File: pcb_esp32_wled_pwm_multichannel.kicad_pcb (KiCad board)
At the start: 4 copper layers, 162.6 x 48.3 mm, 93 parts, among them J101 WJ2EDGRC-5.08-4P, J102 WJ2EDGRC-5.08-4P, J103 WJ2EDGRC-5.08-4P, J104 WJ2EDGRC-5.08-4P, J105 Conn_01x05_Male, J106 Conn_01x03_Female, J107 Conn_01x03_Female, J108 Conn_01x02_Female, J109 USB_C_Receptacle_USB2.0, Q101 IRLR8743TRPBF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

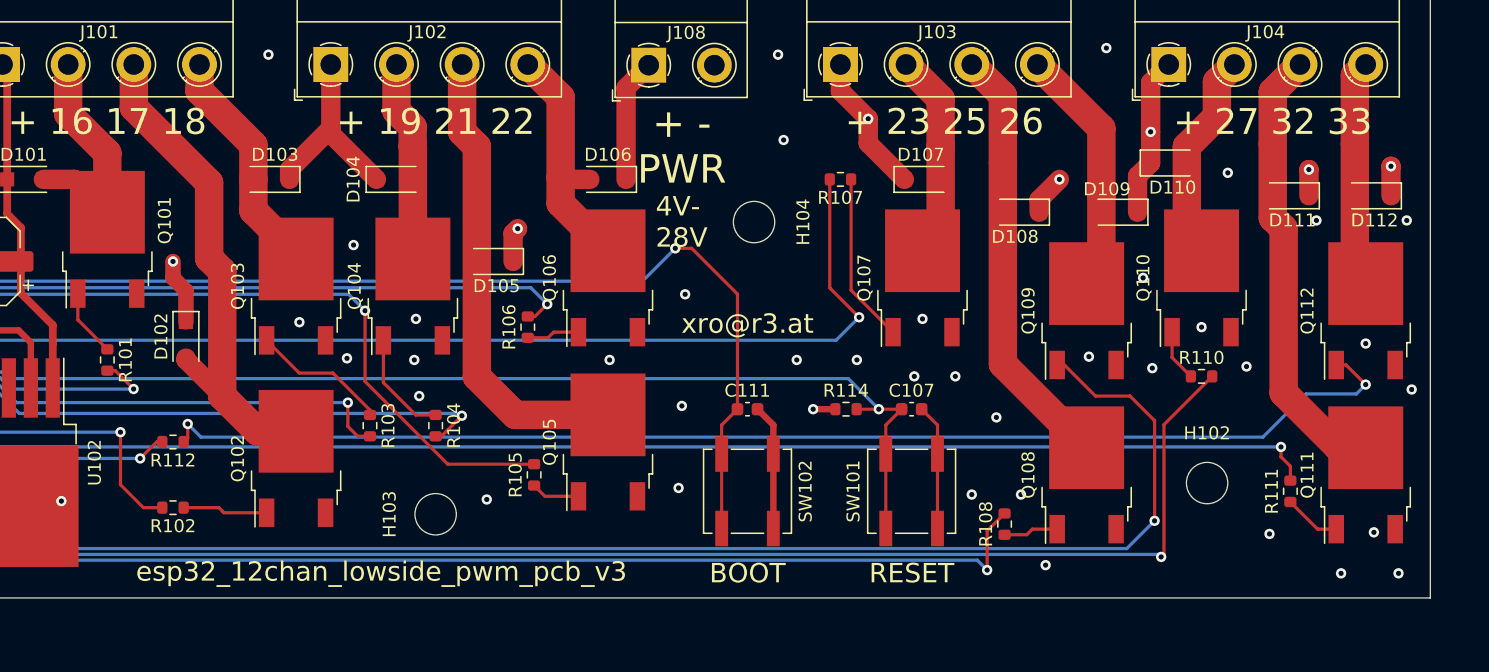
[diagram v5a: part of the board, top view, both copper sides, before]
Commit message: wip: re-add 10ks discharge R to MosFETs
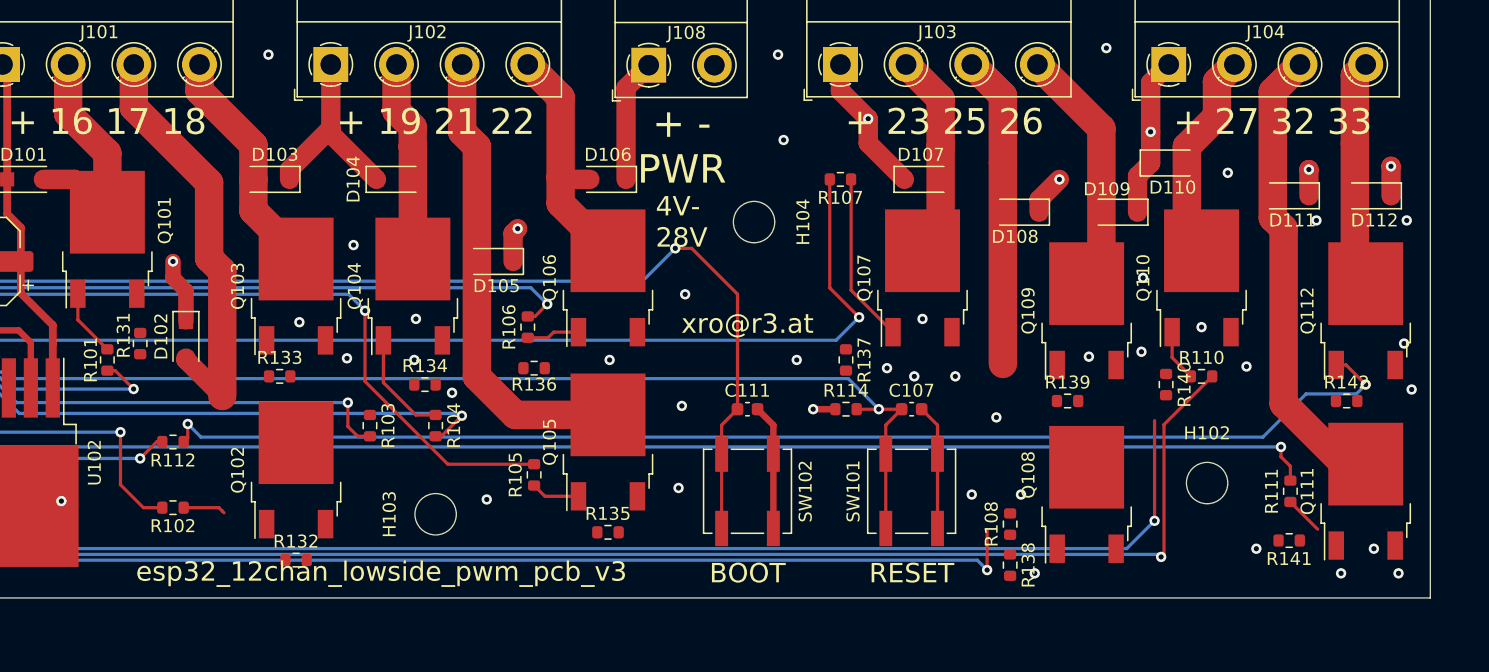
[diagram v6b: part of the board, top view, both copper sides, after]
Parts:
- added R131: 10K(5%), Resistor_SMD:R_0603_1608Metric, F.Cu at (72.4, 66.0)
- added R132: 10K(5%), Resistor_SMD:R_0603_1608Metric, F.Cu at (84.5, 82.8)
- added R133: 10K(5%), Resistor_SMD:R_0603_1608Metric, F.Cu at (83.2, 68.6)
- added R134: 10K(5%), Resistor_SMD:R_0603_1608Metric, F.Cu at (94.4, 69.2)
- added R135: 10K(5%), Resistor_SMD:R_0603_1608Metric, F.Cu at (108.6, 80.6)
- added R136: 10K(5%), Resistor_SMD:R_0603_1608Metric, F.Cu at (102.9, 67.9)
- added R137: 10K(5%), Resistor_SMD:R_0603_1608Metric, F.Cu at (127.0, 67.3)
- added R138: 10K(5%), Resistor_SMD:R_0603_1608Metric, F.Cu at (139.7, 83.2)
- added R139: 10K(5%), Resistor_SMD:R_0603_1608Metric, F.Cu at (144.1, 70.5)
- added R140: 10K(5%), Resistor_SMD:R_0603_1608Metric, F.Cu at (151.8, 69.2)
- added R141: 10K(5%), Resistor_SMD:R_0603_1608Metric, F.Cu at (161.3, 81.3)
- added R142: 10K(5%), Resistor_SMD:R_0603_1608Metric, F.Cu at (165.7, 70.5)
- moved Q108 1.52 mm to (145.6, 77.7)
- moved Q111 1.27 mm to (167.2, 77.5)
- moved Q102 0.88 mm to (84.5, 75.8)
- moved R108 0.43 mm to (139.7, 80.0)
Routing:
- net Net-(Q103-G): track 10.6 -> 0.00 mm
- net Net-(Q109-G): track 142.8 -> 133.5 mm
- net /LED_G3: track 33.3 -> 24.2 mm
- net /LED_G1: track 39.4 -> 32.6 mm
- net Net-(Q108-G): track 4.25 -> 0.00 mm
- net Net-(Q102-G): track 6.58 -> 3.28 mm
- net /PWM_G3: track 123.4 -> 121.5 mm
- net Net-(Q111-G): track 4.42 -> 2.98 mm
- net /LED_G4: track 34.7 -> 35.8 mm

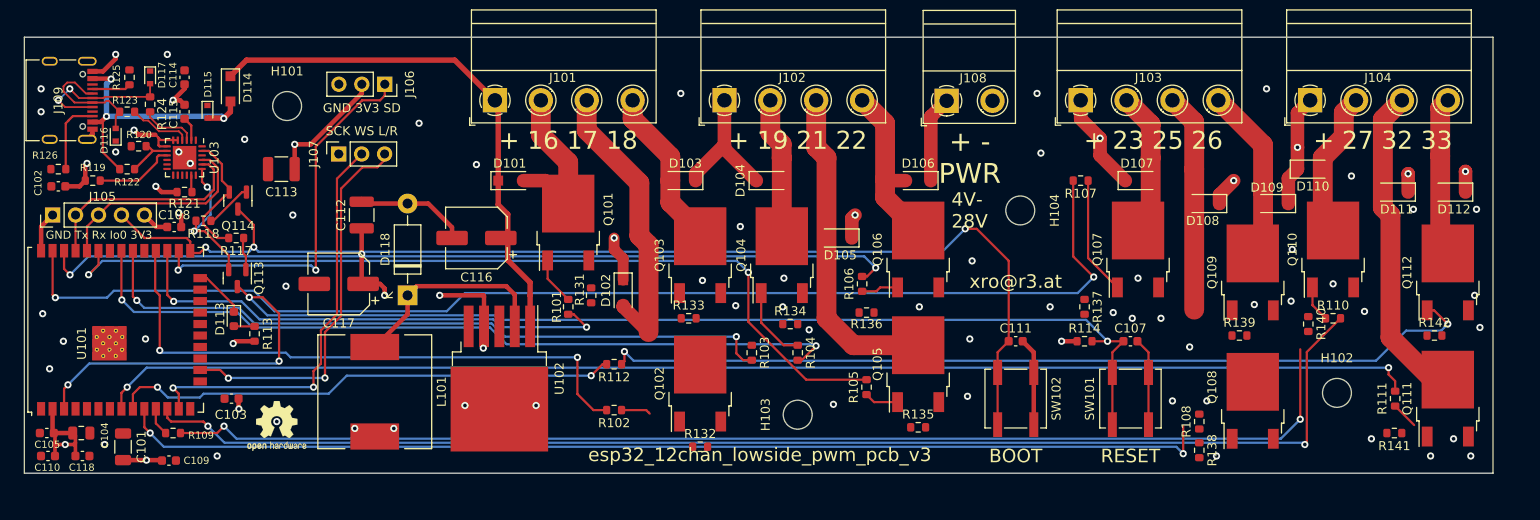
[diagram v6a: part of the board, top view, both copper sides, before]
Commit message: v3 release version: improved routing, closer C, WIP discharge-R done, new renderings, new gerber
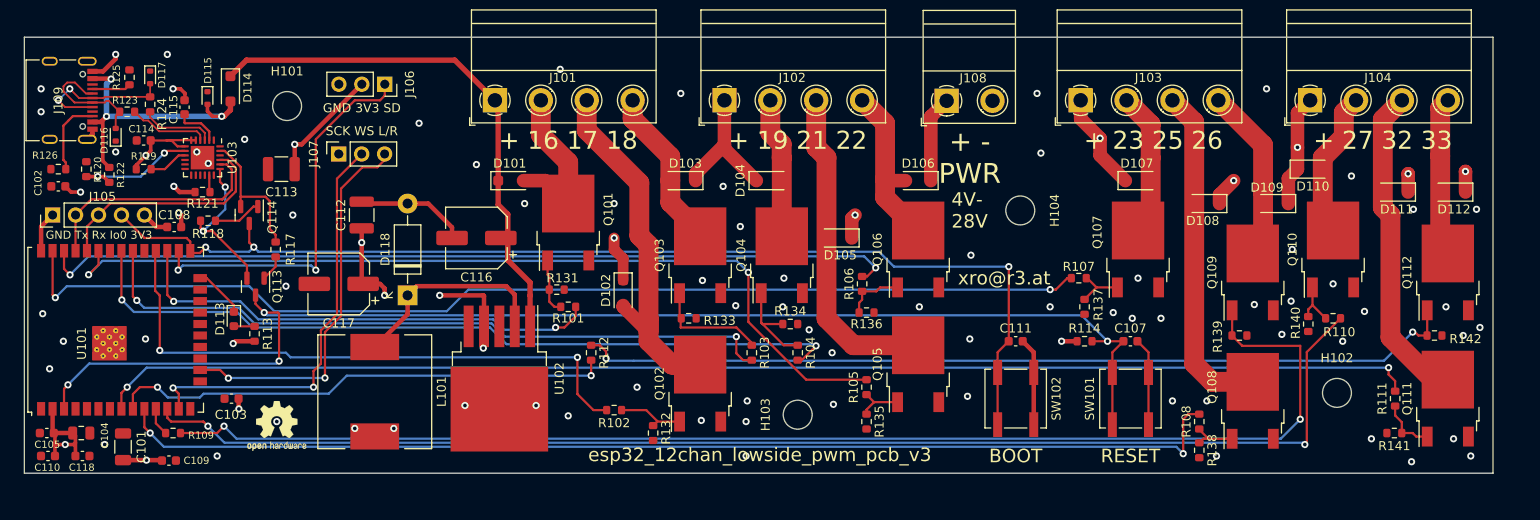
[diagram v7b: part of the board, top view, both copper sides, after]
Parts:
- moved R107 10.8 mm to (126.4, 64.1)
- moved C114 8.32 mm to (22.9, 48.9), turned to 180 degrees
- moved R120 6.32 mm to (16.5, 52.1), turned to 90 degrees
- moved R119 5.78 mm to (22.9, 52.1)
- moved R135 5.75 mm to (102.9, 80.0), turned to -90 degrees
- moved R132 5.42 mm to (79.2, 81.3), turned to -90 degrees
- moved R117 4.55 mm to (37.5, 61.0), turned to 90 degrees
- moved R131 3.86 mm to (68.6, 65.4), turned to 0 degrees
- moved R112 2.84 mm to (72.4, 72.4), turned to -90 degrees
- moved Q113 2.22 mm to (35.2, 65.1)
- moved R122 2.08 mm to (19.1, 52.7), turned to 90 degrees
- moved Q114 2.04 mm to (34.5, 57.1)
- moved R121 1.99 mm to (29.4, 54.6)
- moved U103 1.99 mm to (29.4, 50.8)
- moved D115 1.52 mm to (29.9, 44.2)
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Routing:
- net /PWM_R3: track 134.4 -> 120.7 mm
- net /LED_G3: track 24.2 -> 37.5 mm
- net Net-(Q103-G): track 0.00 -> 12.8 mm
- net Net-(Q109-G): track 133.5 -> 144.7 mm
- net /LED_G1: track 32.6 -> 41.9 mm
- net /VBUS: track 5.39 -> 13.6 mm, vias 0 -> 2
- net Net-(Q107-G): track 13.2 -> 5.75 mm
- net Net-(Q108-G): track 0.00 -> 5.33 mm
- net /IO0: track 127.7 -> 123.1 mm
- net Net-(U103-~{RST}): track 8.90 -> 4.38 mm
- net Net-(Q102-G): track 3.28 -> 7.61 mm
- net /ESP_EN: track 148.4 -> 144.2 mm
- net Net-(Q111-G): track 2.98 -> 6.26 mm
- net /PWM_G3: track 121.5 -> 124.3 mm
- net Net-(Q106-G): track 4.11 -> 6.59 mm
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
